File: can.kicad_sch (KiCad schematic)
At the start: 3 parts, among them J11 PinHeader_2x3_P2.54mm_Drill1.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, U19 TCAN3414DR, U20 TCAN3414DR

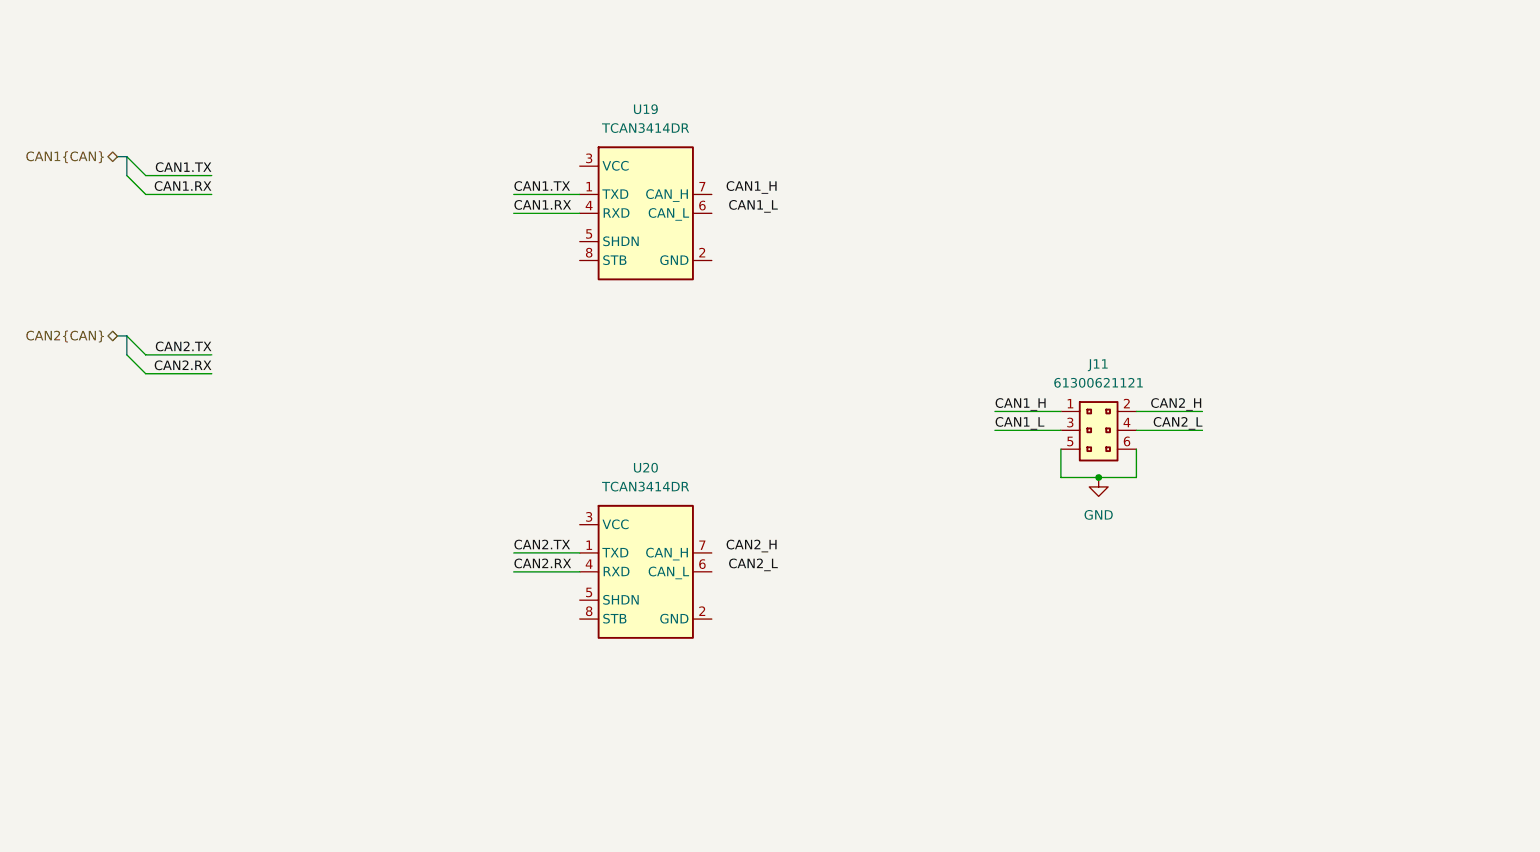
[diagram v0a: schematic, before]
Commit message: [#95036] Add CAN bus subsheet
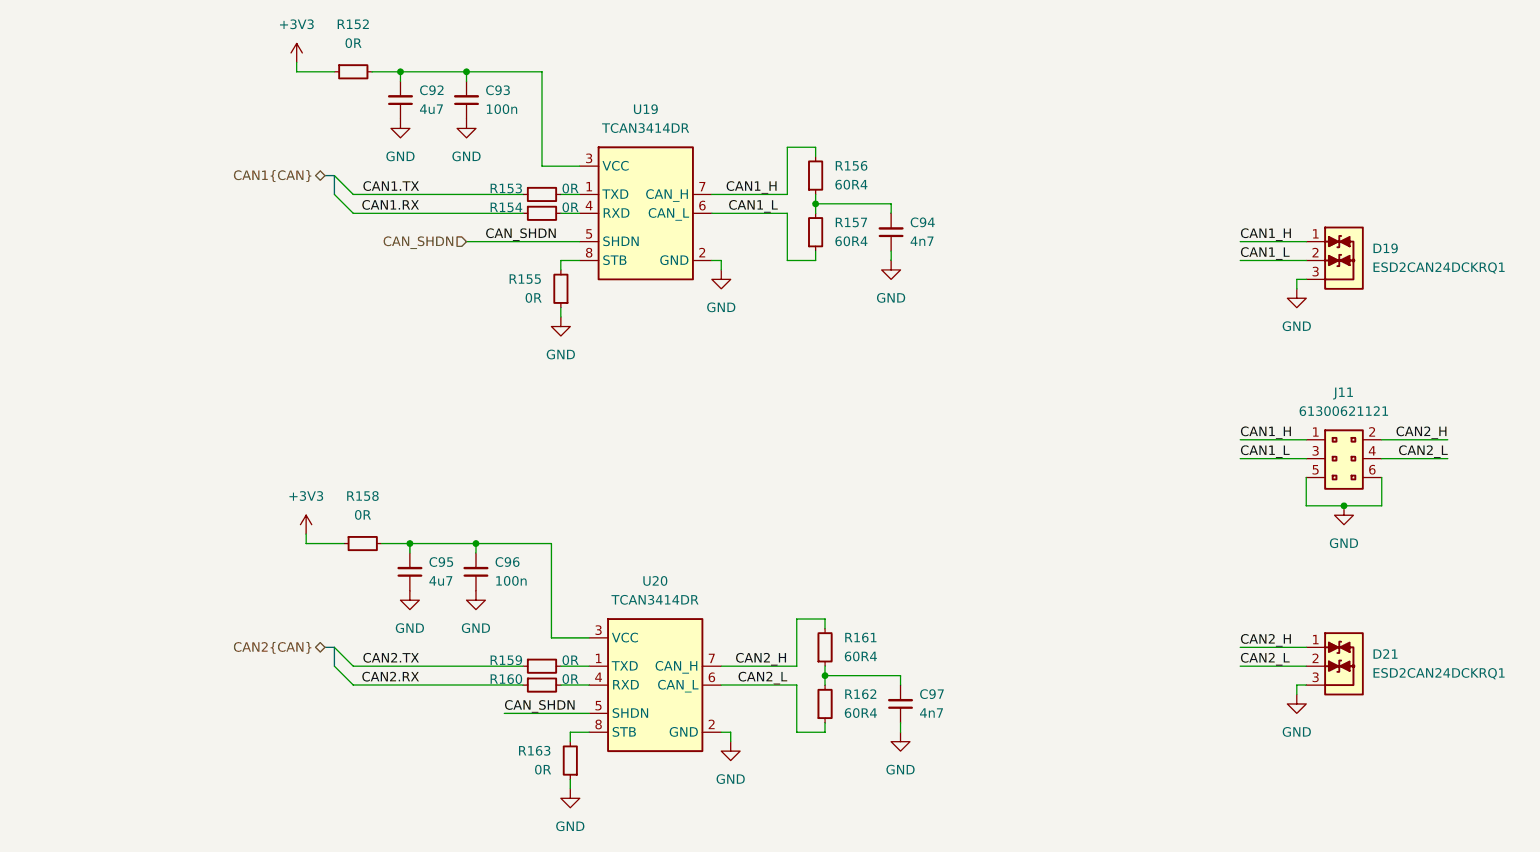
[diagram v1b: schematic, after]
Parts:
- added C92, C95: C_4u7_0402, antmicro-footprints:C_0402_1005Metric, symbol antmicroCapacitors0402:C_4u7_0402
- added C93, C96: C_100n_0402, antmicro-footprints:C_0402_1005Metric, symbol antmicroCapacitors0402:C_100n_0402
- added C94, C97: C_4n7_0402, antmicro-footprints:C_0402_1005Metric, symbol antmicroCapacitors0402:C_4n7_0402
- added D19, D21: ESD2CAN24DCKRQ1, antmicro-footprints:SC70-3, symbol antmicroTVSDiodes:ESD2CAN24DCKRQ1
- added R152, R153, R154, R155, R158, R159, R160, R163: R_0R_0402, antmicro-footprints:R_0402_1005Metric, symbol antmicroResistors0402:R_0R_0402
- added R156, R157, R161, R162: R_60R4_0402, antmicro-footprints:R_0402_1005Metric, symbol antmicroResistors0402:R_60R4_0402
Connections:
- net CAN1.RX: now also R154.1; no longer U19.4 (RXD)
- net CAN1.TX: now also R153.1; no longer U19.1 (TXD)
- net CAN1_H: now also U19.7 (CAN_H), D19.1, R156.2
- net CAN1_L: now also U19.6 (CAN_L), D19.2, R157.1
- net CAN2.RX: now also R160.1; no longer U20.4 (RXD)
- net CAN2.TX: now also R159.1; no longer U20.1 (TXD)
- net CAN2_H: now also U20.7 (CAN_H), D21.1, R161.2
- net CAN2_L: now also U20.6 (CAN_L), D21.2, R162.1
- net GND: now also U19.2 (GND), U20.2 (GND), C92.1, C93.1, C94.1, C95.1, C96.1, C97.1, D19.3, D21.3, R155.1, R163.1
- net at U19.3 (VCC): now also C92.2, C93.2, R152.2
- net CAN_SHDN: now reaches U19.5 (SHDN)
- net CAN_SHDN: now also U20.5 (SHDN)
- net at U19.8 (STB): now also R155.2
- net at U20.3 (VCC): now also C95.2, C96.2, R158.2
- net at U20.8 (STB): now also R163.2
- new net: R159.2, U20.1 (TXD)
- new net: R160.2, U20.4 (RXD)
- new net: C97.2, R161.1, R162.2
- new net: C94.2, R156.1, R157.2
- new net: R153.2, U19.1 (TXD)
- new net: R154.2, U19.4 (RXD)
- new net +3V3: R152.1, R158.1
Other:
- moved on the sheet: J11, U20

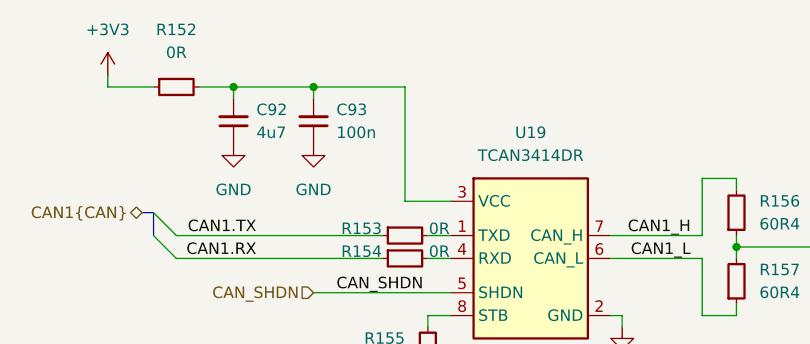
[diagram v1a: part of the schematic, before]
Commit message: [#95036] Solve basic ERCs
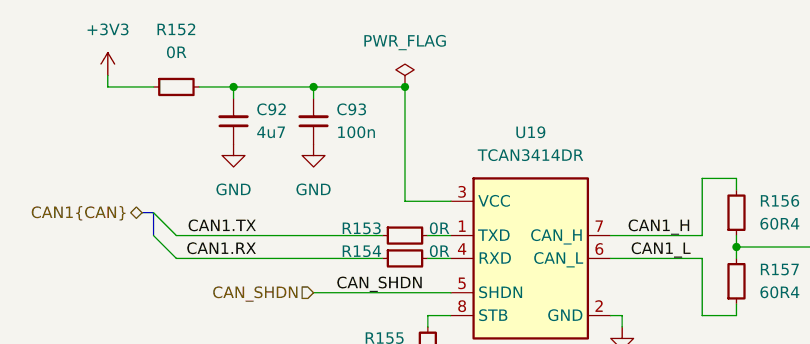
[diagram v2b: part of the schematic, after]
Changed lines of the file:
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@@
+	)
+	(junction
+		(at 123.19 43.18)
+		(diameter 0)
+		(color 0 0 0 0)
 	)
 	(junction
@@
 					(unit 1)
 				)
+			)
+		)
+	)
+	(symbol
+		(lib_id "antmicropower:PWR_FLAG")
+		(at 123.19 43.18 0)
+		(mirror y)
+		(unit 1)
+		(exclude_from_sim no)
+		(in_bom yes)
+		(on_board yes)
+		(dnp no)
+		(fields_autoplaced yes)
+		(property "Reference" "#FLG011"
+			(at 123.19 41.275 0)
+			(effects
+				(font
+					(size 1.27 1.27)
+				)
+				(hide yes)
+			)
+		)
+		(property "Value" "PWR_FLAG"
+			(at 123.19 38.1 0)
+			(effects
+				(font
+					(size 1.27 1.27)
+				)
+			)
+		)
+		(property "Footprint" ""
+			(at 123.19 43.18 0)
+			(effects
+				(font
+					(size 1.27 1.27)
+				)
+				(hide yes)
+			)
+		)
+		(property "Datasheet" ""
+			(at 123.19 43.18 0)
+			(effects
+				(font
+					(size 1.27 1.27)
+				)
+				(hide yes)
+			)
+		)
+		(property "Description" ""
+			(at 123.19 45.72 0)
+			(effects
+				(font
+					(size 1.27 1.27)
+				)
+				(justify left bottom)
+				(hide yes)
+			)
+		)
+		(pin "1"
+		)
+		(instances
+			(project "renode-reference-platform"
+				(path "/126ae87b-f292-4372-94ff-ae46971d67ab/6d40ac90-618b-4fed-a40d-8d6baabd0d71"
+					(reference "#FLG011")
+					(unit 1)
+				)

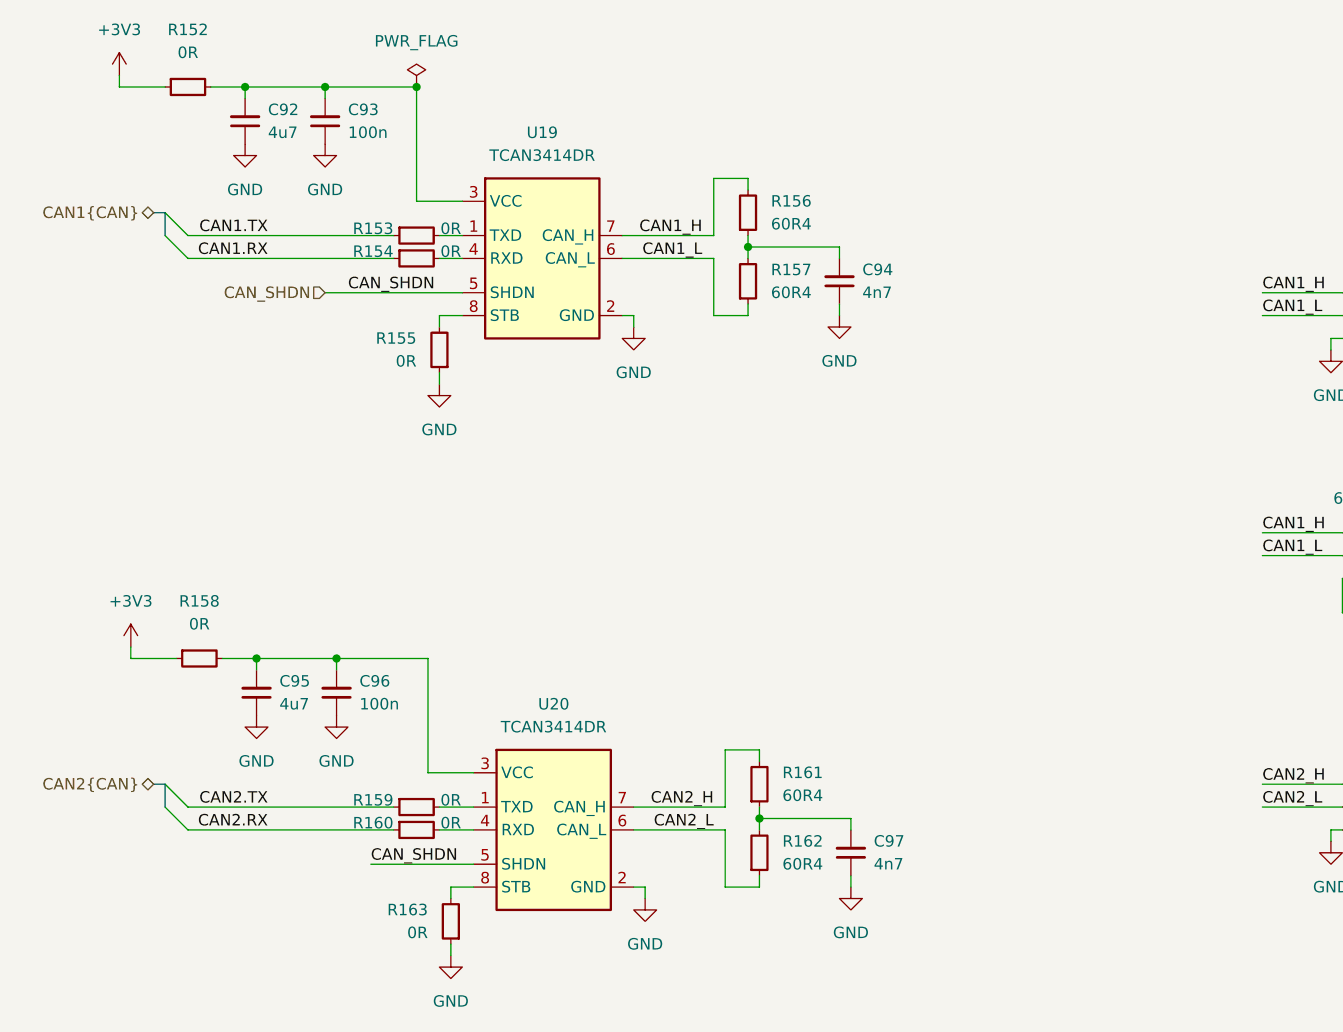
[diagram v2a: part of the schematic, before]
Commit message: [#95036] Fix hierarchical ports directions, add CAN termination jumper
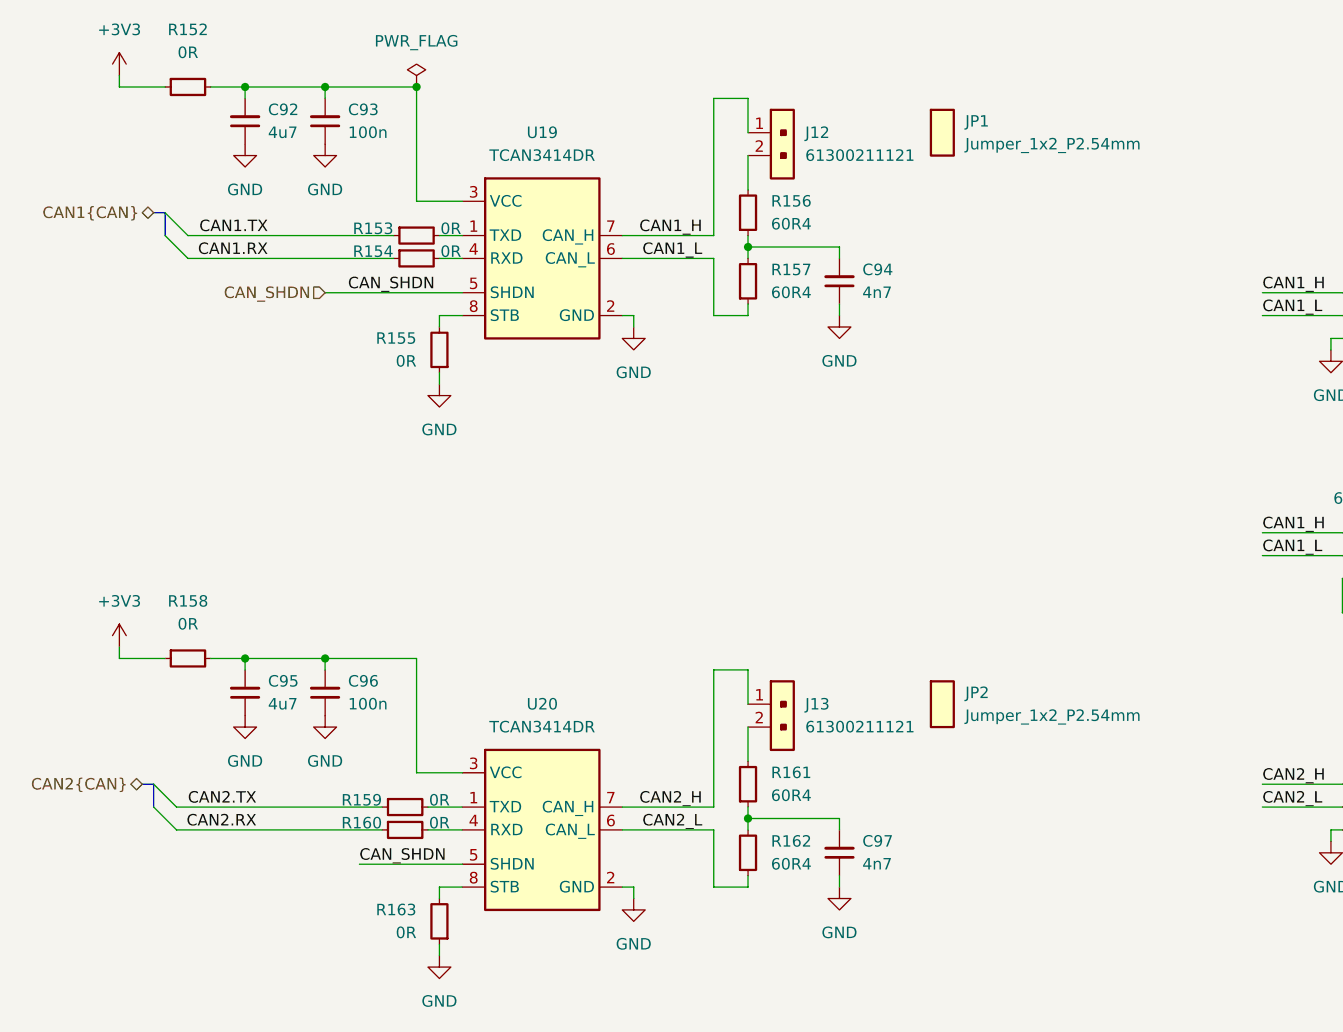
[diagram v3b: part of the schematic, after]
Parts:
- added J12, J13: PinHeader_1x2_P2.54mm_Drill1.1mm, antmicro-footprints:PinHeader_1x2_P2.54_Drill1.1mm, symbol antmicroGenericPinHeaders:PinHeader_1x2_P2.54mm_Drill1.1mm
- added JP1, JP2: Jumper_1x2_P2.54mm, antmicro-footprints:Jumper_1x2_P2.54mm, symbol antmicroShuntsJumpers:Jumper_1x2_P2.54mm
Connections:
- net CAN1_H: now also J12.1; no longer R156.2
- net CAN2_H: now also J13.1; no longer R161.2
- new net: J13.2, R161.2
- new net: J12.2, R156.2
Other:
- moved on the sheet: C95, C96, C97, R158, R159, R160, R161, R162, R163, U20

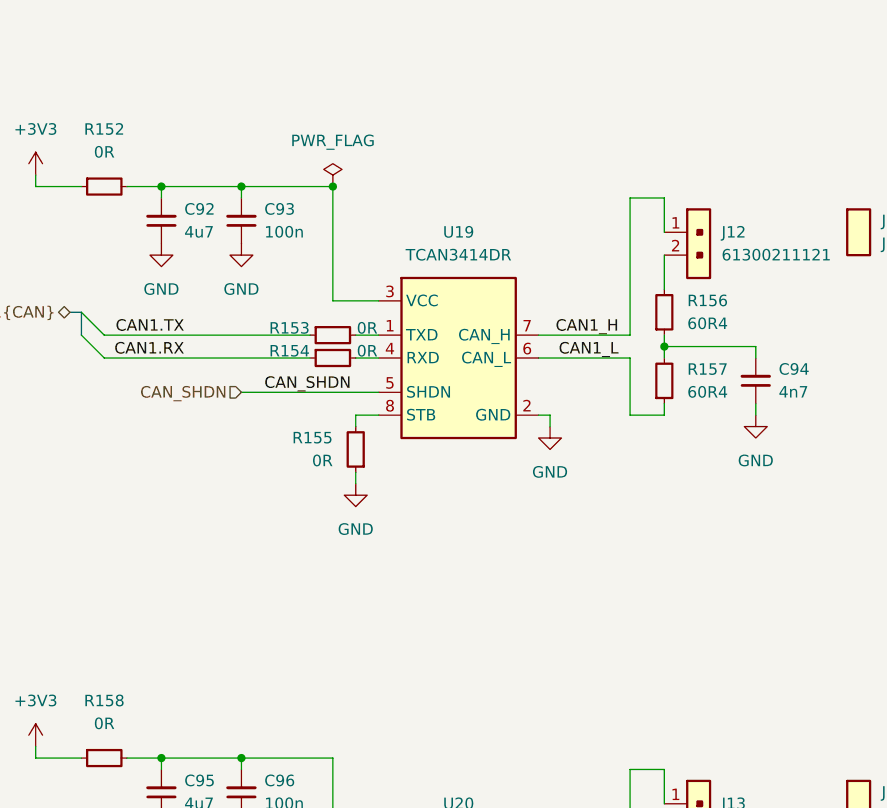
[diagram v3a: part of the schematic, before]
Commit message: [#95036] Add schematic markings
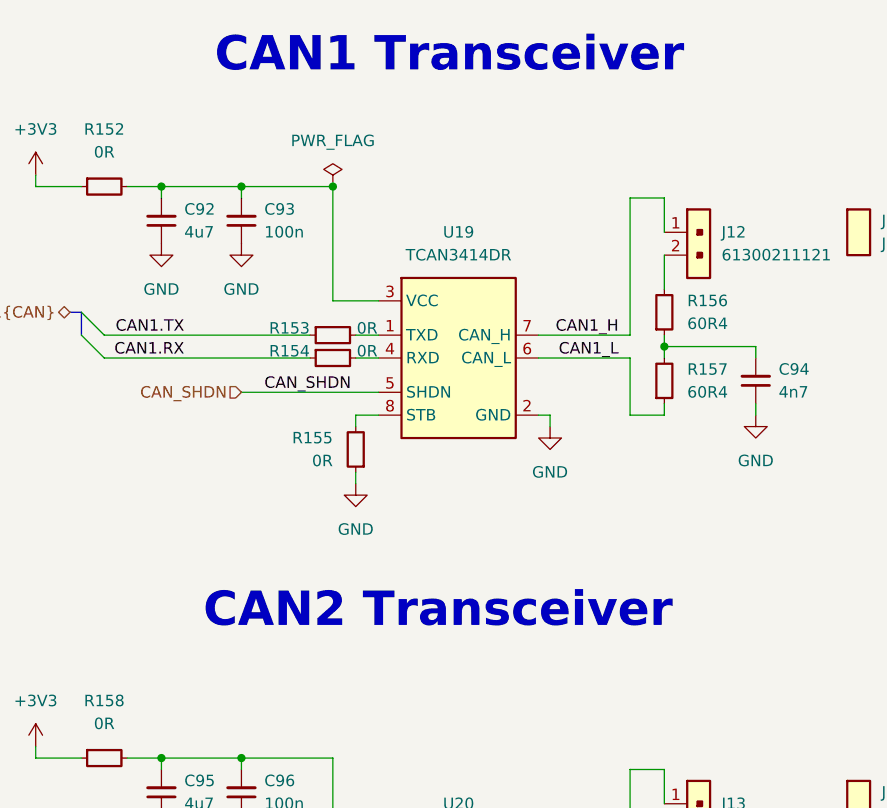
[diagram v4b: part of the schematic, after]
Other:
- note added: "CAN1 Transceiver"
- note added: "CAN2 Transceiver"
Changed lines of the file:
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@@
 		(company "Antmicro")
+	)
+	(text "CAN2 Transceiver"
+		(exclude_from_sim no)
+		(at 134.874 88.138 0)
+		(effects
+			(font
+				(size 3.81 3.81)
+				(thickness 0.762)
+				(bold yes)
+			)
+			(justify top)
+		)
+	)
+	(text "CAN1 Transceiver"
+		(exclude_from_sim no)
+		(at 136.144 26.416 0)
+		(effects
+			(font
+				(size 3.81 3.81)
+				(thickness 0.762)
+				(bold yes)
+			)
+			(justify top)
+		)
 	)
 	(junction

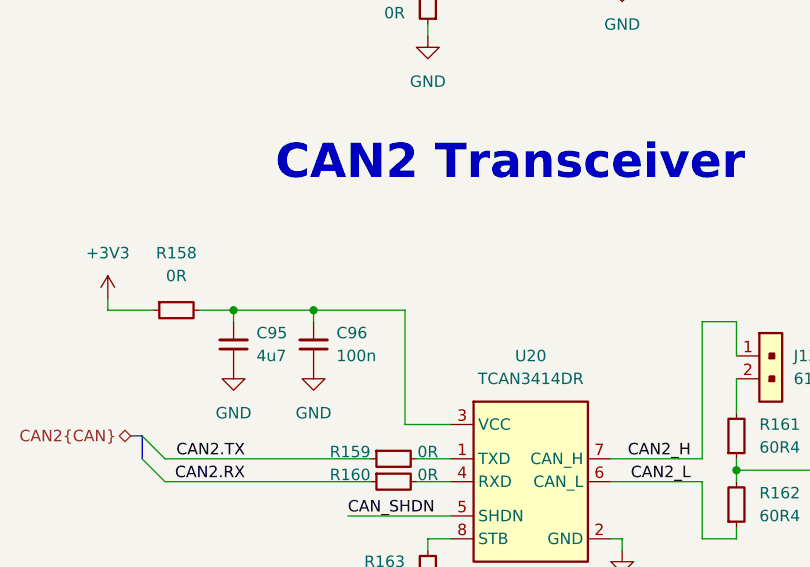
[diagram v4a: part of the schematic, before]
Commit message: [#95036] Solve ERC
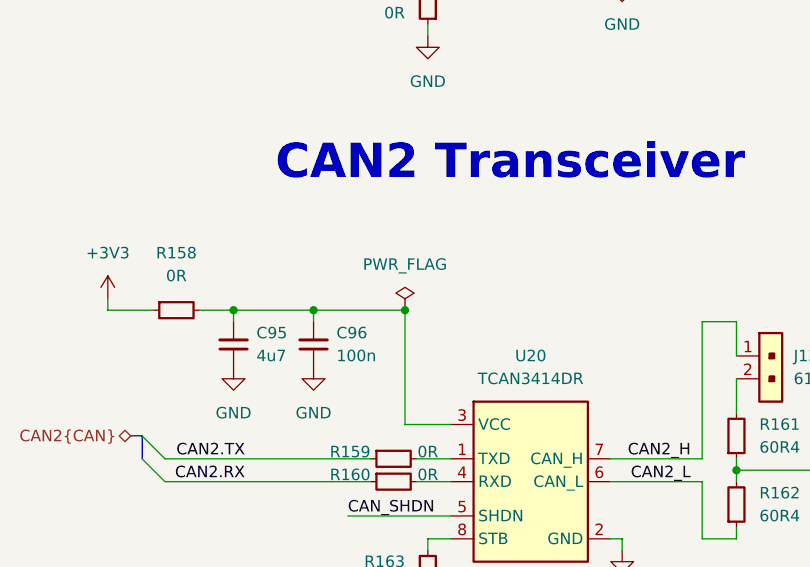
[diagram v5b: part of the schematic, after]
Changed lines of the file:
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@@
 	)
 	(junction
+		(at 123.19 106.68)
+		(diameter 0)
+		(color 0 0 0 0)
+	)
+	(junction
 		(at 231.14 101.6)
 		(diameter 0)
@@
 					(unit 1)
 				)
+			)
+		)
+	)
+	(symbol
+		(lib_id "antmicropower:PWR_FLAG")
+		(at 123.19 106.68 0)
+		(mirror y)
+		(unit 1)
+		(exclude_from_sim no)
+		(in_bom yes)
+		(on_board yes)
+		(dnp no)
+		(fields_autoplaced yes)
+		(property "Reference" "#FLG016"
+			(at 123.19 104.775 0)
+			(effects
+				(font
+					(size 1.27 1.27)
+				)
+				(hide yes)
+			)
+		)
+		(property "Value" "PWR_FLAG"
+			(at 123.19 101.6 0)
+			(effects
+				(font
+					(size 1.27 1.27)
+				)
+			)
+		)
+		(property "Footprint" ""
+			(at 123.19 106.68 0)
+			(effects
+				(font
+					(size 1.27 1.27)
+				)
+				(hide yes)
+			)
+		)
+		(property "Datasheet" ""
+			(at 123.19 106.68 0)
+			(effects
+				(font
+					(size 1.27 1.27)
+				)
+				(hide yes)
+			)
+		)
+		(property "Description" ""
+			(at 123.19 109.22 0)
+			(effects
+				(font
+					(size 1.27 1.27)
+				)
+				(justify left bottom)
+				(hide yes)
+			)
+		)
+		(pin "1"
+		)
+		(instances
+			(project "renode-reference-platform"
+				(path "/126ae87b-f292-4372-94ff-ae46971d67ab/6d40ac90-618b-4fed-a40d-8d6baabd0d71"
+					(reference "#FLG016")
+					(unit 1)
+				)
